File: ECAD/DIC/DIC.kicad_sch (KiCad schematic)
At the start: 66 parts, among them J2 Conn_02x05_Top_Bottom, J3 Conn_02x05_Top_Bottom, J4 Conn_02x05_Top_Bottom, J5 Conn_02x05_Top_Bottom, U1 R-78E5.0-1.0, U2 MCP130-270, U3 STM32F072RBTx, U5 R-78E3.3-1.0, U7 MCP2562-E-SN, U8 NCP1117-12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

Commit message: production ready
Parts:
- removed R49, R51, R53, R54: 20R 0603, Resistor_SMD:R_0603_1608Metric_Pad0.98x0.95mm_HandSolder, symbol Device:R
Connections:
- net CAN_RX: now also U7.4 (RXD)
- net CAN_TX: now also U3.45 (PA12)
- net SPI1_MOSI_Display: now also U3.23 (PA7)
- net SPI1_SCK_Display: now also U3.21 (PA5)
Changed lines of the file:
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@@
     (stroke (width 0) (type default))
   )
-  (wire (pts (xy 116.84 62.23) (xy 121.92 62.23))
-    (stroke (width 0) (type default))
-  )
   (wire (pts (xy 170.18 111.76) (xy 170.18 121.92))
     (stroke (width 0) (type default))
@@
     (stroke (width 0) (type default))
   )
-  (wire (pts (xy 116.84 80.01) (xy 120.65 80.01))
+  (wire (pts (xy 116.84 80.01) (xy 149.86 80.01))
     (stroke (width 0) (type default))
   )
@@
     (stroke (width 0) (type default))
   )
-  (wire (pts (xy 217.17 83.82) (xy 218.44 83.82))
-    (stroke (width 0) (type default))
-  )
   (wire (pts (xy 217.17 107.95) (xy 231.14 107.95))
     (stroke (width 0) (type default))
@@
     (stroke (width 0) (type default))
   )
-  (wire (pts (xy 129.54 67.31) (xy 158.75 67.31))
+  (wire (pts (xy 116.84 67.31) (xy 158.75 67.31))
     (stroke (width 0) (type default))
   )
@@
     (stroke (width 0) (type default))
   )
+  (wire (pts (xy 198.12 83.82) (xy 218.44 83.82))
+    (stroke (width 0) (type default))
+  )
   (wire (pts (xy 198.12 81.28) (xy 218.44 81.28))
     (stroke (width 0) (type default))
@@
     (stroke (width 0) (type default))
   )
-  (wire (pts (xy 198.12 83.82) (xy 209.55 83.82))
-    (stroke (width 0) (type default))
-  )
   (wire (pts (xy 276.86 139.7) (xy 262.89 139.7))
     (stroke (width 0) (type default))
@@
     (stroke (width 0) (type default))
   )
-  (wire (pts (xy 128.27 80.01) (xy 149.86 80.01))
-    (stroke (width 0) (type default))
-  )
   (wire (pts (xy 170.18 121.92) (xy 173.99 121.92))
     (stroke (width 0) (type default))
@@
     (stroke (width 0) (type default))
   )
-  (wire (pts (xy 129.54 62.23) (xy 158.75 62.23))
+  (wire (pts (xy 116.84 62.23) (xy 158.75 62.23))
     (stroke (width 0) (type default))
   )
@@
     (stroke (width 0) (type default))
   )
-  (wire (pts (xy 116.84 67.31) (xy 121.92 67.31))
-    (stroke (width 0) (type default))
-  )
   (wire (pts (xy 31.75 76.2) (xy 31.75 72.39))
     (stroke (width 0) (type default))
@@
     )
   )
-  (symbol (lib_id "Device:R") (at 213.36 83.82 270) (unit 1)
-    (in_bom yes) (on_board yes) (dnp no)
-    (property "Reference" "R54" (at 213.36 83.82 90)
-      (effects (font (size 1.27 1.27)))
-    )
-    (property "Value" "20R 0603" (at 213.36 86.36 90)
-      (effects (font (size 1.27 1.27)))
-    )
-    (property "Footprint" "Resistor_SMD:R_0603_1608Metric_Pad0.98x0.95mm_HandSolder" (at 213.36 82.042 90)
-      (effects (font (size 1.27 1.27)) hide)
-    )
-    (property "Datasheet" "~" (at 213.36 83.82 0)
-      (effects (font (size 1.27 1.27)) hide)
-    )
-    (pin "1")
-    (pin "2")
-    (instances
-      (project "DIC"
-        (path "/64369a6c-13db-47f8-8de7-12b4f0b9bc27"
-          (reference "R54") (unit 1)
-        )
-      )
-    )
-  )
   (symbol (lib_id "power:GND") (at 93.98 29.21 270) (unit 1)
     (in_bom yes) (on_board yes) (dnp no)
@@
     )
   )
-  (symbol (lib_id "Device:R") (at 124.46 80.01 270) (unit 1)
-    (in_bom yes) (on_board yes) (dnp no)
-    (property "Reference" "R53" (at 124.46 80.01 90)
-      (effects (font (size 1.27 1.27)))
-    )
-    (property "Value" "20R 0603" (at 133.35 78.74 90)
-      (effects (font (size 1.27 1.27)))
-    )
-    (property "Footprint" "Resistor_SMD:R_0603_1608Metric_Pad0.98x0.95mm_HandSolder" (at 124.46 78.232 90)
-      (effects (font (size 1.27 1.27)) hide)
-    )
-    (property "Datasheet" "~" (at 124.46 80.01 0)
-      (effects (font (size 1.27 1.27)) hide)
-    )
-    (pin "1")
-    (pin "2")
-    (instances
-      (project "DIC"
-        (path "/64369a6c-13db-47f8-8de7-12b4f0b9bc27"
-          (reference "R53") (unit 1)
-        )
-      )
-    )
-  )
   (symbol (lib_id "power:+BATT") (at 90.17 171.45 90) (unit 1)
     (in_bom yes) (on_board yes) (dnp no) (fields_autoplaced)
@@
     )
   )
-  (symbol (lib_id "Device:R") (at 125.73 62.23 270) (unit 1)
-    (in_bom yes) (on_board yes) (dnp no)
-    (property "Reference" "R49" (at 125.73 62.23 90)
-      (effects (font (size 1.27 1.27)))
-    )
-    (property "Value" "20R 0603" (at 133.35 60.96 90)
-      (effects (font (size 1.27 1.27)))
-    )
-    (property "Footprint" "Resistor_SMD:R_0603_1608Metric_Pad0.98x0.95mm_HandSolder" (at 125.73 60.452 90)
-      (effects (font (size 1.27 1.27)) hide)
-    )
-    (property "Datasheet" "~" (at 125.73 62.23 0)
-      (effects (font (size 1.27 1.27)) hide)
-    )
-    (pin "1")
-    (pin "2")
-    (instances
-      (project "DIC"
-        (path "/64369a6c-13db-47f8-8de7-12b4f0b9bc27"
-          (reference "R49") (unit 1)
-        )
-      )
-    )
-  )
   (symbol (lib_id "Device:D_Schottky") (at 260.35 83.82 0) (unit 1)
     (in_bom yes) (on_board yes) (dnp no)
@@
         )
       )
-    )
-  )
-  (symbol (lib_id "Device:R") (at 125.73 67.31 270) (unit 1)
-    (in_bom yes) (on_board yes) (dnp no)
-    (property "Reference" "R51" (at 125.73 67.31 90)
-      (effects (font (size 1.27 1.27)))
-    )
-    (property "Value" "20R 0603" (at 133.35 66.04 90)
-      (effects (font (size 1.27 1.27)))
-    )
-    (property "Footprint" "Resistor_SMD:R_0603_1608Metric_Pad0.98x0.95mm_HandSolder" (at 125.73 65.532 90)
-      (effects (font (size 1.27 1.27)) hide)
-    )
-    (property "Datasheet" "~" (at 125.73 67.31 0)
-      (effects (font (size 1.27 1.27)) hide)
-    )
-    (pin "1")
-    (pin "2")
-    (instances
-      (project "DIC"
-        (path "/64369a6c-13db-47f8-8de7-12b4f0b9bc27"
-          (reference "R51") (unit 1)
-        )
-      )

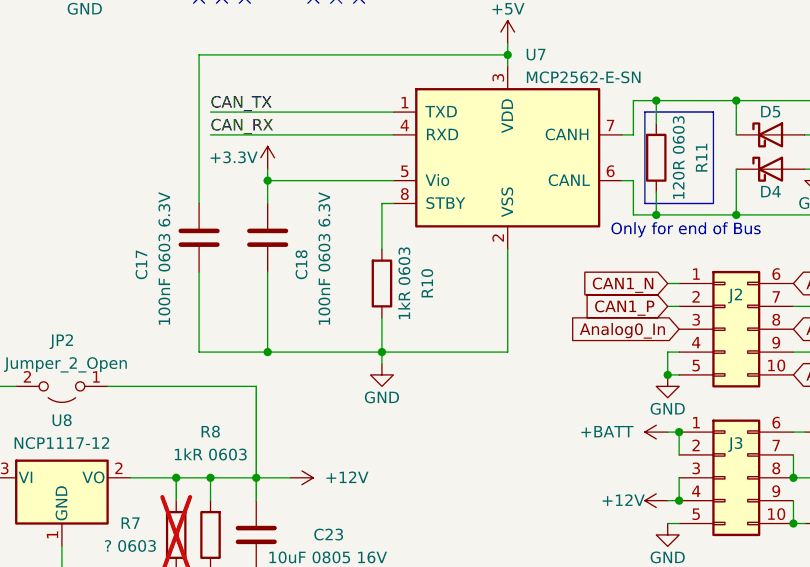
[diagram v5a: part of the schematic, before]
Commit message: bunch o SW
added all baseline code for Display LED, ADC etc.
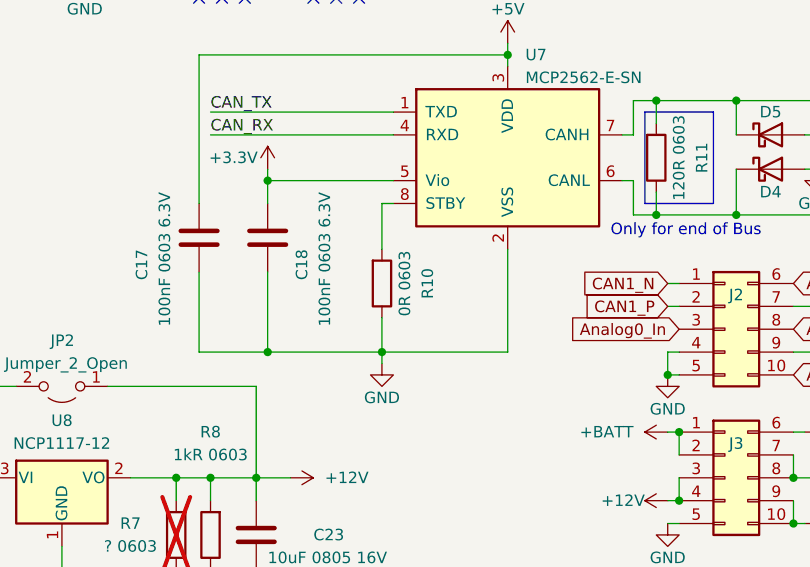
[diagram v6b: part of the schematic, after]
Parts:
- R10: value 1kR 0603 -> 0R 0603
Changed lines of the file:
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@@
       (effects (font (size 1.27 1.27)))
     )
-    (property "Value" "1kR 0603" (at 219.71 100.33 90)
+    (property "Value" "0R 0603" (at 219.71 100.33 90)
       (effects (font (size 1.27 1.27)))
     )
